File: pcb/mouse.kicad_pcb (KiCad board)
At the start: 2 copper layers, 90 x 45 mm, 69 parts, among them J1 USB_C_Receptacle_USB2.0, J2 Conn_01x05, J3 Conn_02x03_Counter_Clockwise, J4 Conn_01x06, J5 Conn_01x06, SW1 SW_Push_SPDT, SW2 SW_Push_SPDT, SW3 SW_Push_SPDT, SW4 SW_Push_SPDT, SW5 RotaryEncoder, SW6 SW_Push, U1 pmw3360-t2qu, U2 TLV70018_SOT23-5, U3 STM32F042K6Tx, U4 TLV70033_SOT23-5

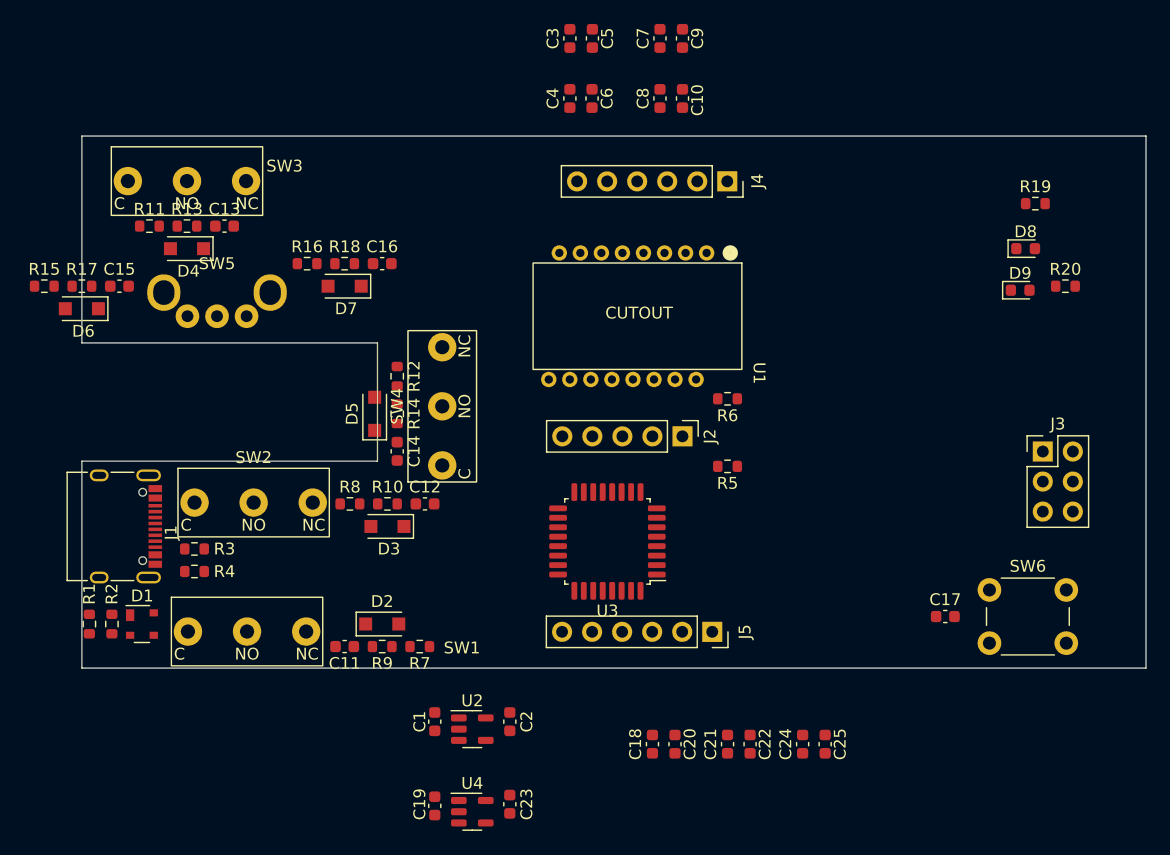
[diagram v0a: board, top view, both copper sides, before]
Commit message: - added boot select resistor - regenerated netlist - adjusted pcb component placement
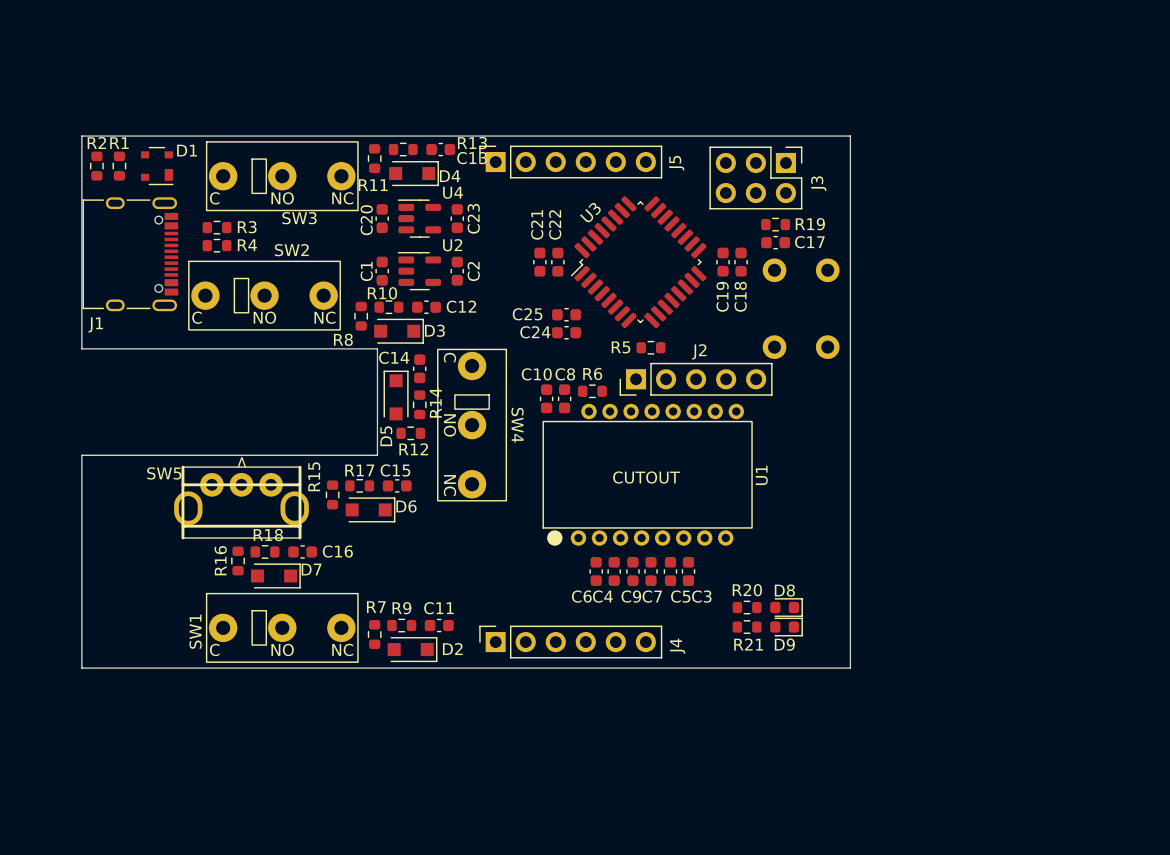
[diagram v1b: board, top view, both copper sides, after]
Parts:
- added R19: 10k, Resistor_SMD:R_0603_1608Metric, F.Cu at (236.5, 82.4)
- SW6: moved to B.Cu
- moved U4 50.4 mm to (206.4, 81.9)
- moved C20 49.9 mm to (203.2, 81.9), turned to 90 degrees
- moved C23 49.7 mm to (209.6, 81.9)
- moved C3 46.2 mm to (229.1, 111.8), turned to -90 degrees
- moved C5 45.6 mm to (227.6, 111.8), turned to -90 degrees
- moved C9 45.3 mm to (224.4, 111.8), turned to -90 degrees
- moved C7 45.1 mm to (225.9, 111.8), turned to -90 degrees
- moved C22 43.9 mm to (218.1, 85.6)
- moved J5 43.8 mm to (212.8, 77.1), turned to 90 degrees
- moved C21 43.7 mm to (216.5, 85.6)
- moved J4 43.6 mm to (212.8, 117.7), turned to 90 degrees
- moved C25 42.4 mm to (218.8, 90.0), turned to 180 degrees
- moved R20 42.0 mm to (234.1, 114.8)
- moved C18 41.4 mm to (233.6, 85.6), turned to -90 degrees
- moved C19 41.0 mm to (232.0, 85.6), turned to -90 degrees
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- renumbered C20 to C19, C19 to C20, R19 to R20, R20 to R21
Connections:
- U3 pad 31: /mcu/BOOT0 -> Net-(R19-Pad2)
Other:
- board size 90 x 45 mm -> 65 x 45 mm

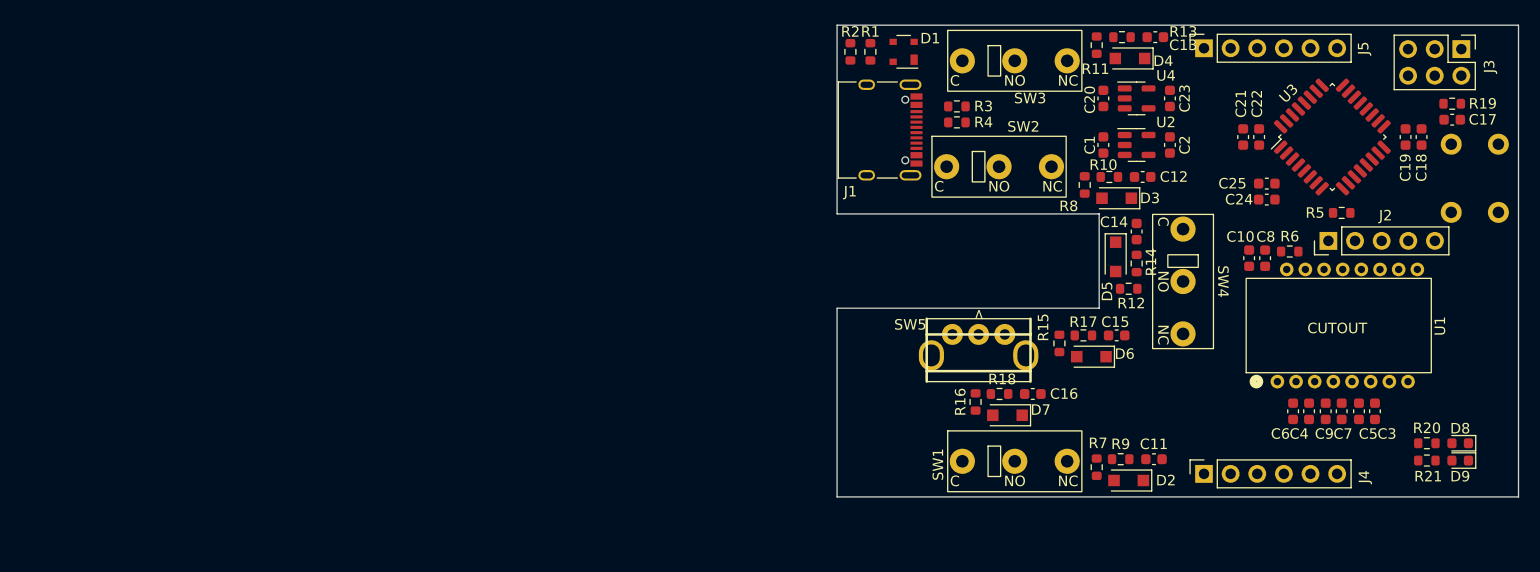
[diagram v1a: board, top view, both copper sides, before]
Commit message: connected all pcb elements with tracks
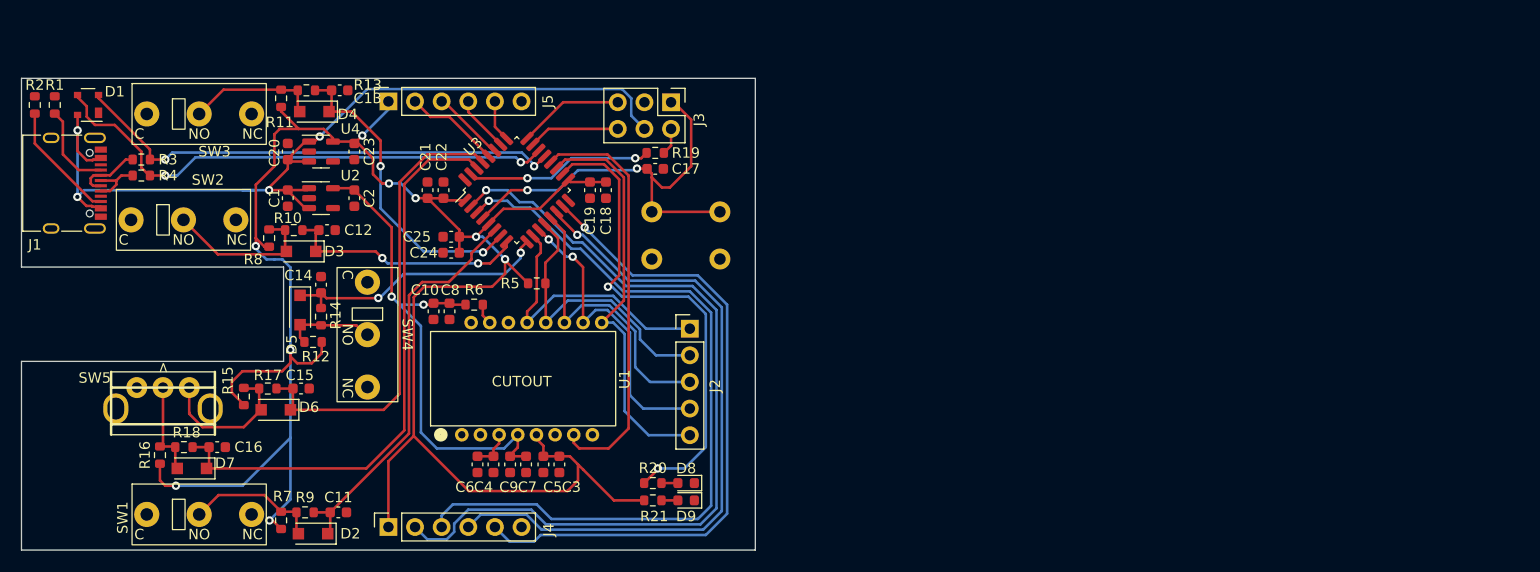
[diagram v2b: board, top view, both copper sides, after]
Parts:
- moved SW6 80.9 mm to (160.1, 97.2), turned to 0 degrees
- moved C11 78.0 mm to (130.2, 121.4)
- moved C12 78.0 mm to (129.1, 94.5)
- moved C14 78.0 mm to (128.6, 99.7)
- moved C18 78.0 mm to (155.8, 90.7)
- moved C2 78.0 mm to (131.8, 91.4)
- moved C22 78.0 mm to (140.3, 90.7)
- moved C23 78.0 mm to (131.8, 87.0)
- moved C3 78.0 mm to (151.3, 116.8)
- moved C4 78.0 mm to (145.0, 116.8)
- moved C5 78.0 mm to (149.8, 116.8)
- moved C6 78.0 mm to (143.5, 116.8)
- moved D1 78.0 mm to (106.3, 82.5)
- moved D4 78.0 mm to (127.9, 83.2)
- moved D7 78.0 mm to (116.3, 117.2)
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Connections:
- J5 pad 2: /mcu/PB3 -> /mcu/PB5
- J5 pad 4: /mcu/PB5 -> /mcu/PB3
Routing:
- net +3V3: track 0.00 -> 202.4 mm, vias 0 -> 9
- net +5V: track 0.00 -> 87.2 mm, vias 0 -> 4
- net /mcu/PF0: track 0.00 -> 79.8 mm, vias 0 -> 1
- net /mcu/PF1: track 0.00 -> 74.0 mm, vias 0 -> 1
- net /mcu/PB0: track 0.00 -> 65.1 mm, vias 0 -> 1
- net /mcu/PB1: track 0.00 -> 63.4 mm, vias 0 -> 1
- net /buttons/ZB: track 0.00 -> 55.8 mm
- net /mcu/USB_DP: track 0.00 -> 50.2 mm, vias 0 -> 2
- net +1V8: track 0.00 -> 48.6 mm, vias 0 -> 2
- net /mcu/LED: track 0.00 -> 47.5 mm, vias 0 -> 2
- net /mcu/USB_DM: track 0.00 -> 47.1 mm, vias 0 -> 2
- net /buttons/ZA: track 0.00 -> 44.3 mm
- net /mcu/RESET: track 0.00 -> 40.5 mm, vias 0 -> 2
- net /mcu/SENSOR_RESET: track 0.00 -> 39.7 mm
- net /mcu/SENSOR_MOTION: track 0.00 -> 39.4 mm
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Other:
- board size 65 x 45 mm -> 70 x 45 mm

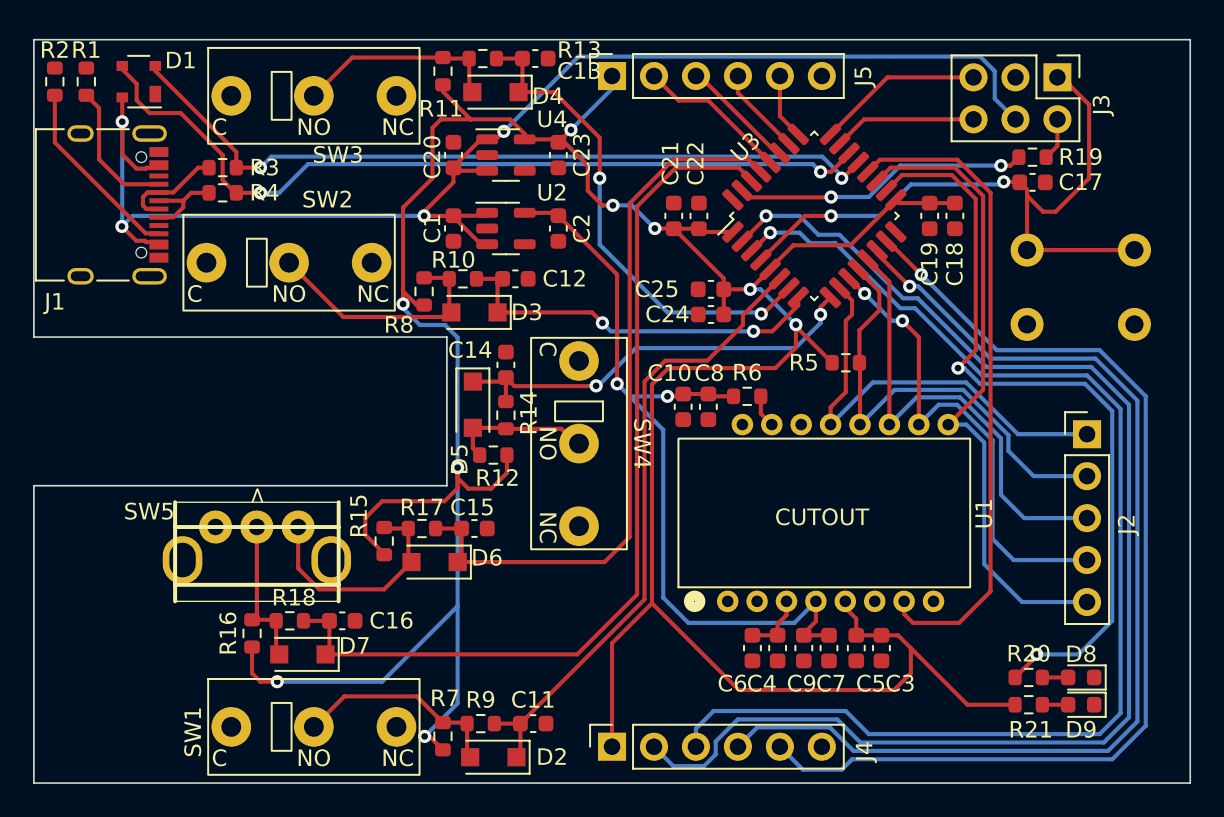
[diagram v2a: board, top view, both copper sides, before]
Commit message: added pcb mounting holes
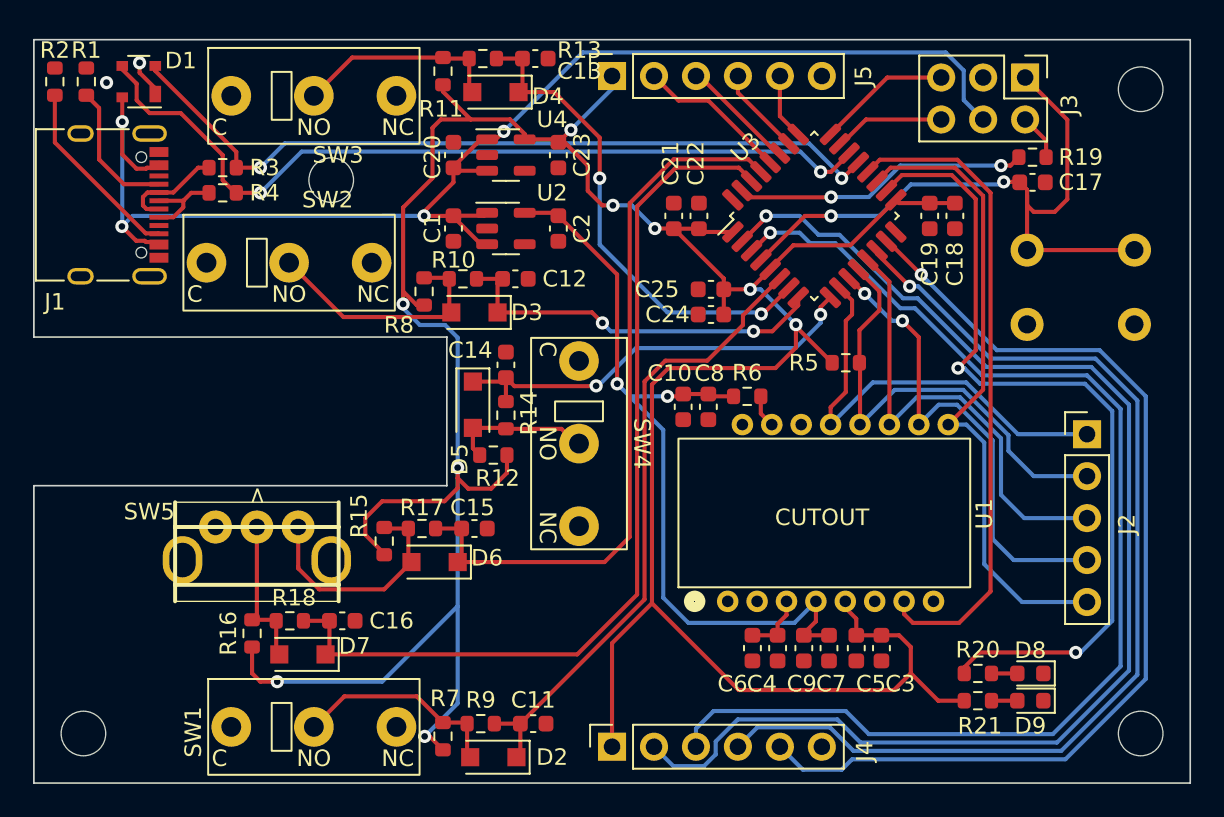
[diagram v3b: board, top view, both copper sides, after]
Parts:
- added REF**: MountingHole_2.7mm_M2.5, MountingHole:MountingHole_2.7mm_M2.5, F.Cu at (167.0, 122.0)
- added REF**: MountingHole_2.7mm_M2.5, MountingHole:MountingHole_2.7mm_M2.5, F.Cu at (118.0, 88.5)
- added REF**: MountingHole_2.7mm_M2.5, MountingHole:MountingHole_2.7mm_M2.5, F.Cu at (103.0, 122.0)
- added REF**: MountingHole_2.7mm_M2.5, MountingHole:MountingHole_2.7mm_M2.5, F.Cu at (167.0, 83.0)
- moved D8 3.09 mm to (160.3, 118.4)
- moved D9 3.09 mm to (160.3, 120.0)
- moved R20 3.09 mm to (157.1, 118.4)
- moved R21 3.09 mm to (157.1, 120.0)
- moved J3 1.96 mm to (160.0, 82.3)
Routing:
- net +3V3: track 202.4 -> 198.6 mm
- net /mcu/LED: track 47.5 -> 50.7 mm
- net GND: track 0.00 -> 2.28 mm, vias 0 -> 2
- net /mcu/SWDIO: track 8.71 -> 6.75 mm
- net /mcu/SWCLK: track 10.1 -> 8.14 mm
- net +5V: track 87.2 -> 85.5 mm
- net /mcu/PF0: track 79.8 -> 78.2 mm
- net /mcu/PB1: track 63.4 -> 61.7 mm
- net /mcu/PF1: track 74.0 -> 72.3 mm
- net /mcu/PB0: track 65.1 -> 63.4 mm
- net /mcu/USB_DM: track 47.1 -> 47.8 mm
- net /mcu/USB_DP: track 50.2 -> 50.8 mm

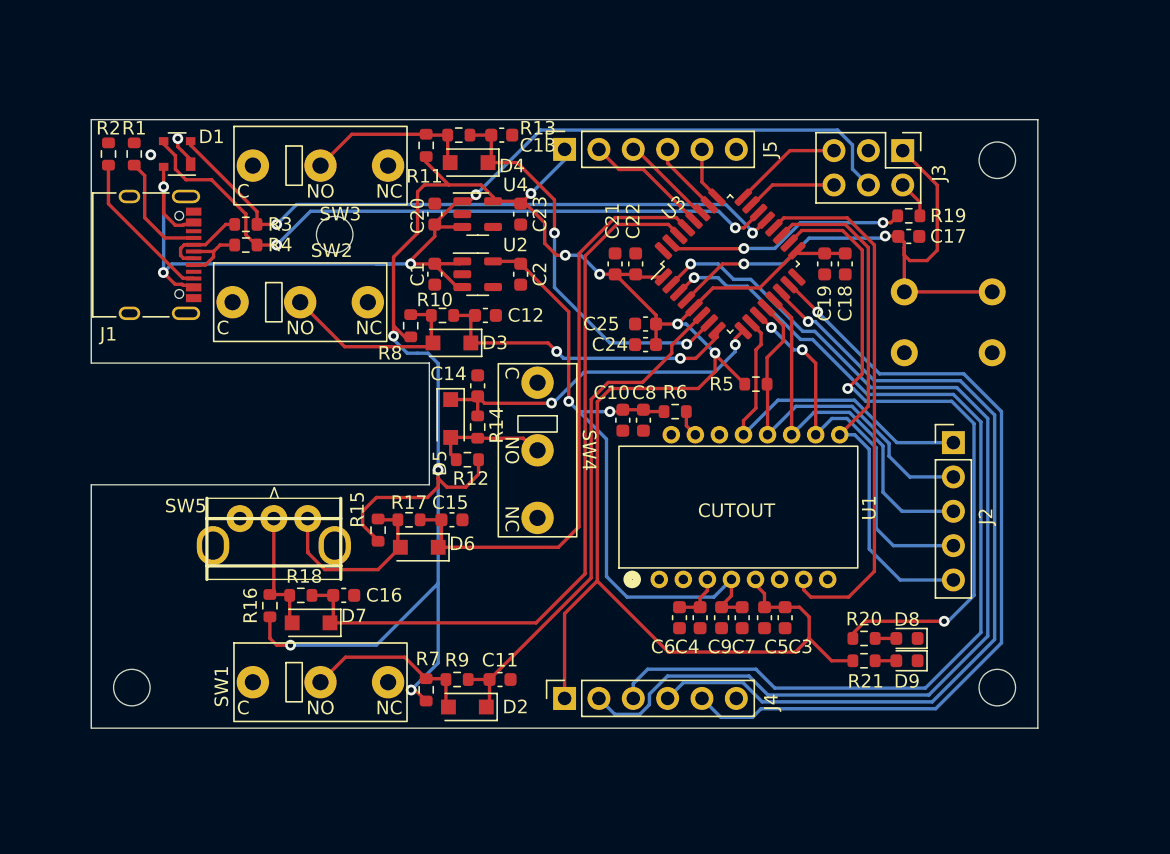
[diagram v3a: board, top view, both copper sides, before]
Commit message: fixed pcb according to DRC check
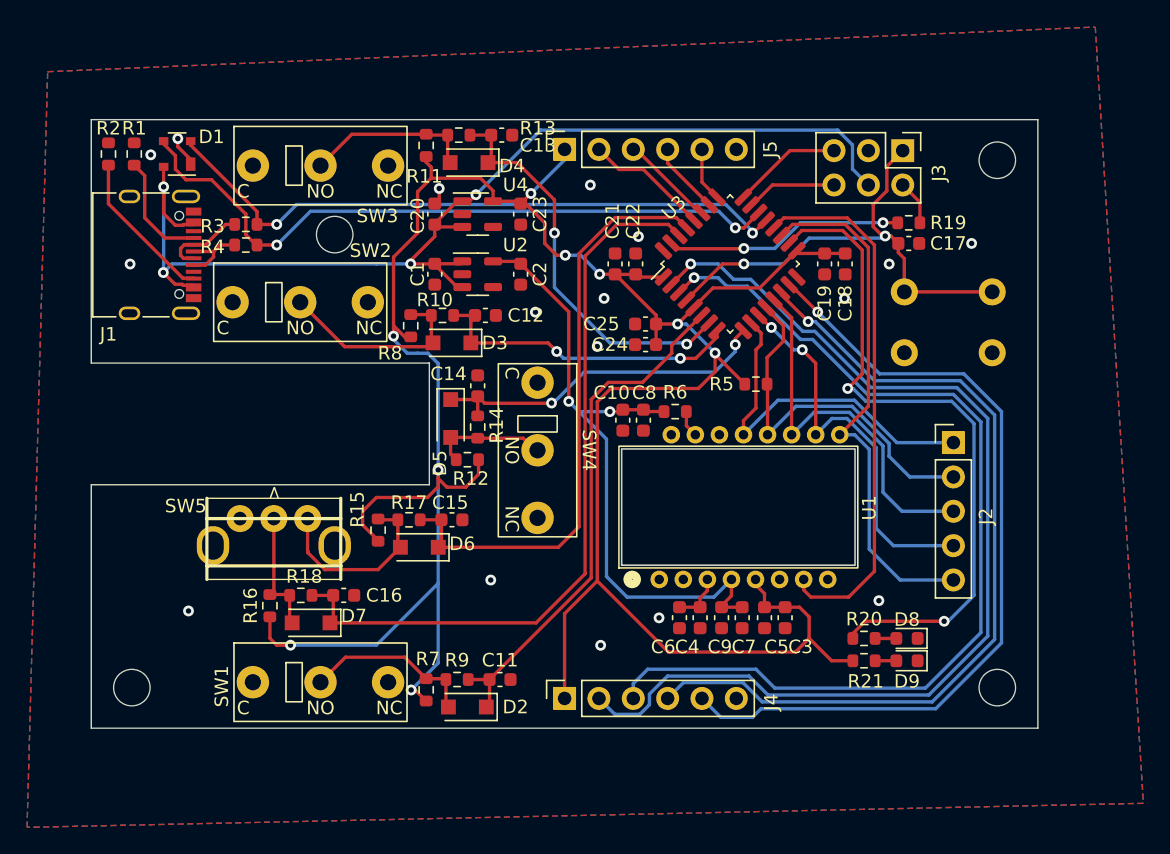
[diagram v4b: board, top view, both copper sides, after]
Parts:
- moved C17 0.52 mm to (160.5, 89.2)
- moved R19 0.52 mm to (160.5, 87.6)
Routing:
- net /mcu/RESET: track 40.3 -> 35.8 mm
- net GND: track 2.28 -> 3.54 mm, vias 2 -> 17
- net +5V: track 85.5 -> 84.4 mm
- net /mcu/BOOT0: track 2.81 -> 3.33 mm
- added copper zone on B.Cu, net GND
- added copper zone on F.Cu, net GND
